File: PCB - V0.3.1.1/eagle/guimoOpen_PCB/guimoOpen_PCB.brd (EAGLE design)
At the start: 45.7 x 73.7 mm, 8 parts, among them M1 ARDUINO-NANO-3.0, U1 GY-521MPU6050

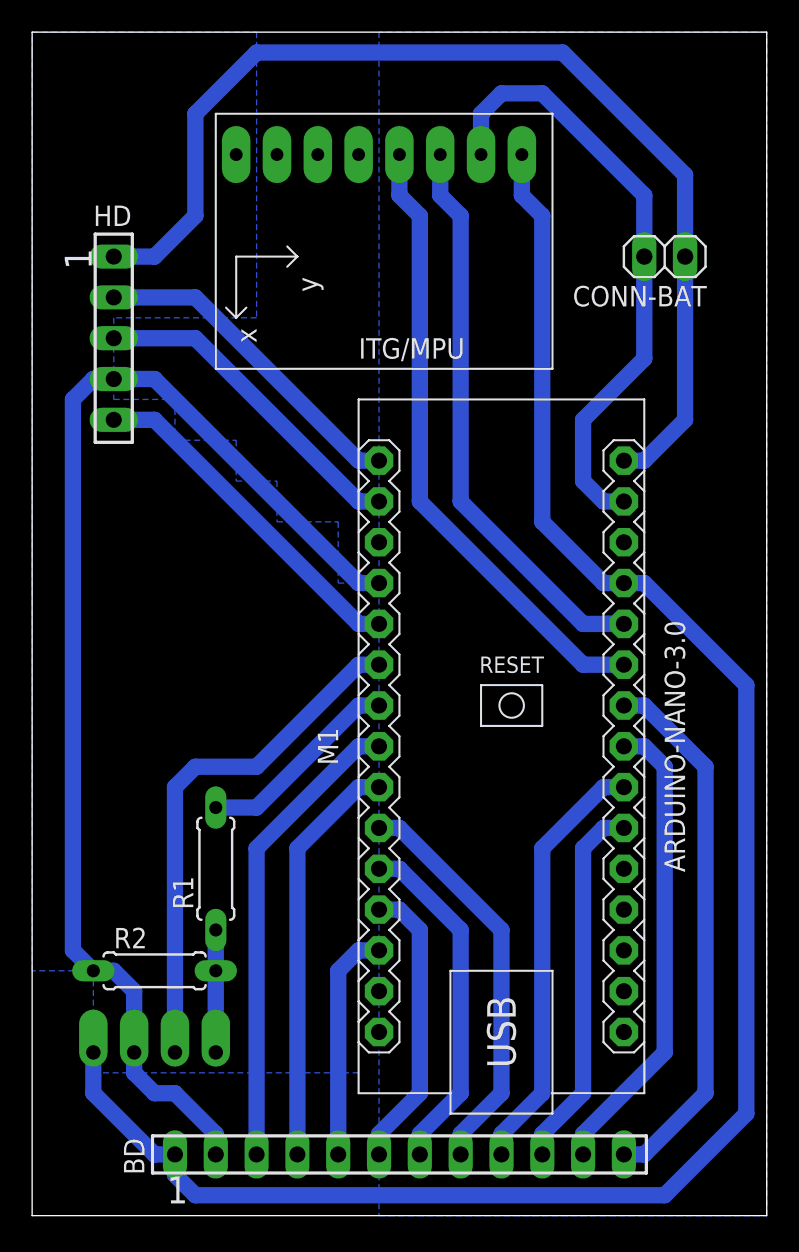
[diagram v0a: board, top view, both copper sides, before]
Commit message: Correção do roteamento do acelerômetro. SDA e SCL foram colocadas nas portas A4 e A5
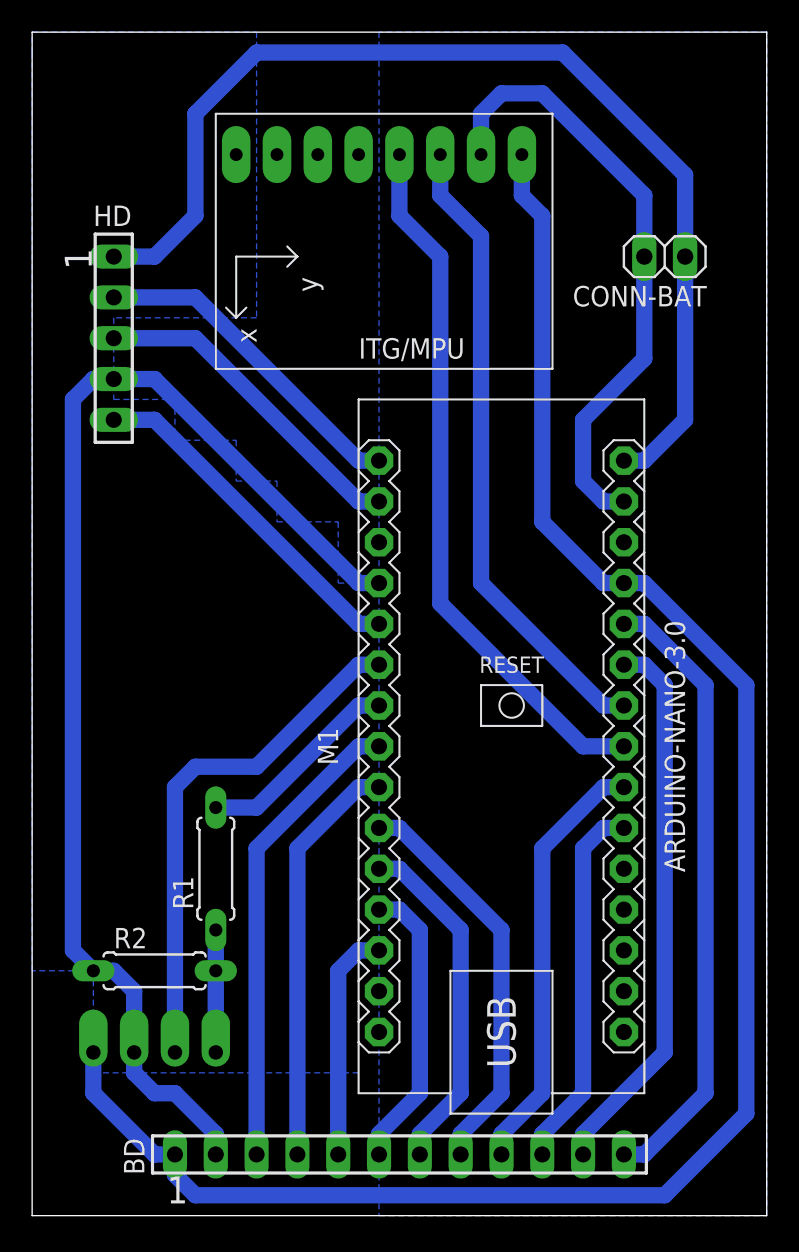
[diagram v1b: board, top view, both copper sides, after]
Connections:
- net N$15: now also M1.J2.5; no longer M1.J2.7
- net N$16: now also M1.J2.6; no longer M1.J2.8
- net N$3: now also M1.J2.7; no longer M1.J2.5
- net N$4: now also M1.J2.8; no longer M1.J2.6
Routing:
- net N$15: track 33.6 -> 38.7 mm
- net N$4: track 39.0 -> 44.1 mm
- net N$16: track 29.3 -> 34.4 mm
- net N$3: track 36.7 -> 39.8 mm
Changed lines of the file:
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@@
 <layer number="17" name="Pads" color="2" fill="1" visible="yes" active="yes"/>
 <layer number="18" name="Vias" color="2" fill="1" visible="yes" active="yes"/>
-<layer number="19" name="Unrouted" color="6" fill="1" visible="yes" active="yes"/>
+<layer number="19" name="Unrouted" color="6" fill="1" visible="no" active="yes"/>
 <layer number="20" name="Dimension" color="15" fill="1" visible="yes" active="yes"/>
-<layer number="21" name="tPlace" color="7" fill="1" visible="yes" active="yes"/>
-<layer number="22" name="bPlace" color="7" fill="1" visible="yes" active="yes"/>
-<layer number="23" name="tOrigins" color="15" fill="1" visible="yes" active="yes"/>
-<layer number="24" name="bOrigins" color="15" fill="1" visible="yes" active="yes"/>
-<layer number="25" name="tNames" color="7" fill="1" visible="yes" active="yes"/>
-<layer number="26" name="bNames" color="7" fill="1" visible="yes" active="yes"/>
-<layer number="27" name="tValues" color="7" fill="1" visible="yes" active="yes"/>
-<layer number="28" name="bValues" color="7" fill="1" visible="yes" active="yes"/>
+<layer number="21" name="tPlace" color="7" fill="1" visible="no" active="yes"/>
+<layer number="22" name="bPlace" color="7" fill="1" visible="no" active="yes"/>
+<layer number="23" name="tOrigins" color="15" fill="1" visible="no" active="yes"/>
+<layer number="24" name="bOrigins" color="15" fill="1" visible="no" active="yes"/>
+<layer number="25" name="tNames" color="7" fill="1" visible="no" active="yes"/>
+<layer number="26" name="bNames" color="7" fill="1" visible="no" active="yes"/>
+<layer number="27" name="tValues" color="7" fill="1" visible="no" active="yes"/>
+<layer number="28" name="bValues" color="7" fill="1" visible="no" active="yes"/>
 <layer number="29" name="tStop" color="7" fill="3" visible="no" active="yes"/>
 <layer number="30" name="bStop" color="7" fill="6" visible="no" active="yes"/>
@@
 <layer number="132" name="bAdjust" color="7" fill="1" visible="no" active="yes"/>
 <layer number="144" name="Drill_legend" color="7" fill="1" visible="no" active="yes"/>
-<layer number="150" name="Notes" color="7" fill="1" visible="yes" active="yes"/>
+<layer number="150" name="Notes" color="7" fill="1" visible="no" active="yes"/>
 <layer number="151" name="HeatSink" color="7" fill="1" visible="no" active="yes"/>
 <layer number="152" name="_bDocu" color="7" fill="1" visible="no" active="yes"/>
@@
 <wire x1="20.32" y1="31.75" x2="21.59" y2="31.75" width="1.016" layer="16"/>
 </signal>
-<signal name="N$4">
-<contactref element="U1" pad="SDA"/>
-<contactref element="M1" pad="J2.6"/>
-<wire x1="36.83" y1="34.29" x2="34.29" y2="34.29" width="1.016" layer="16"/>
-<wire x1="34.29" y1="34.29" x2="24.13" y2="44.45" width="1.016" layer="16"/>
-<wire x1="24.13" y1="44.45" x2="24.13" y2="62.23" width="1.016" layer="16"/>
-<wire x1="24.13" y1="62.23" x2="22.86" y2="63.5" width="1.016" layer="16"/>
-<wire x1="22.86" y1="63.5" x2="22.86" y2="66.04" width="1.016" layer="16"/>
-</signal>
 <signal name="N$7">
 <contactref element="HD" pad="1"/>
@@
 <signal name="N$15">
 <contactref element="BD" pad="12"/>
-<contactref element="M1" pad="J2.7"/>
+<contactref element="M1" pad="J2.5"/>
 <wire x1="36.83" y1="3.81" x2="38.1" y2="3.81" width="1.016" layer="16"/>
 <wire x1="38.1" y1="3.81" x2="41.91" y2="7.62" width="1.016" layer="16"/>
-<wire x1="41.91" y1="7.62" x2="41.91" y2="27.94" width="1.016" layer="16"/>
-<wire x1="41.91" y1="27.94" x2="38.1" y2="31.75" width="1.016" layer="16"/>
-<wire x1="38.1" y1="31.75" x2="36.83" y2="31.75" width="1.016" layer="16"/>
+<wire x1="41.91" y1="7.62" x2="41.91" y2="33.02" width="1.016" layer="16"/>
+<wire x1="41.91" y1="33.02" x2="38.1" y2="36.83" width="1.016" layer="16"/>
+<wire x1="38.1" y1="36.83" x2="36.83" y2="36.83" width="1.016" layer="16"/>
 </signal>
 <signal name="N$16">
 <contactref element="BD" pad="11"/>
-<contactref element="M1" pad="J2.8"/>
+<contactref element="M1" pad="J2.6"/>
 <wire x1="34.29" y1="3.81" x2="34.29" y2="5.08" width="1.016" layer="16"/>
 <wire x1="34.29" y1="5.08" x2="39.37" y2="10.16" width="1.016" layer="16"/>
-<wire x1="39.37" y1="10.16" x2="39.37" y2="27.94" width="1.016" layer="16"/>
-<wire x1="39.37" y1="27.94" x2="38.1" y2="29.21" width="1.016" layer="16"/>
-<wire x1="38.1" y1="29.21" x2="36.83" y2="29.21" width="1.016" layer="16"/>
+<wire x1="39.37" y1="10.16" x2="39.37" y2="33.02" width="1.016" layer="16"/>
+<wire x1="39.37" y1="33.02" x2="38.1" y2="34.29" width="1.016" layer="16"/>
+<wire x1="38.1" y1="34.29" x2="36.83" y2="34.29" width="1.016" layer="16"/>
 </signal>
 <signal name="N$19">
@@
 <wire x1="34.29" y1="22.86" x2="35.56" y2="24.13" width="1.016" layer="16"/>
 <wire x1="35.56" y1="24.13" x2="36.83" y2="24.13" width="1.016" layer="16"/>
-</signal>
-<signal name="N$3">
-<contactref element="U1" pad="SCL"/>
-<contactref element="M1" pad="J2.5"/>
-<wire x1="36.83" y1="36.83" x2="35.56" y2="36.83" width="1.016" layer="16"/>
-<wire x1="25.4" y1="66.04" x2="25.4" y2="63.5" width="1.016" layer="16"/>
-<wire x1="25.4" y1="63.5" x2="26.67" y2="62.23" width="1.016" layer="16"/>
-<wire x1="26.67" y1="62.23" x2="26.67" y2="44.45" width="1.016" layer="16"/>
-<wire x1="26.67" y1="44.45" x2="34.29" y2="36.83" width="1.016" layer="16"/>
-<wire x1="34.29" y1="36.83" x2="36.83" y2="36.83" width="1.016" layer="16"/>
 </signal>
 <signal name="N$17">
@@
 <contactref element="M1" pad="J2.14"/>
 </signal>
+<signal name="N$3">
+<contactref element="U1" pad="SCL"/>
+<contactref element="M1" pad="J2.7"/>
+<wire x1="36.83" y1="31.75" x2="35.56" y2="31.75" width="1.016" layer="16"/>
+<wire x1="35.56" y1="31.75" x2="27.94" y2="39.37" width="1.016" layer="16"/>
+<wire x1="27.94" y1="39.37" x2="27.94" y2="60.96" width="1.016" layer="16"/>
+<wire x1="27.94" y1="60.96" x2="25.4" y2="63.5" width="1.016" layer="16"/>
+<wire x1="25.4" y1="63.5" x2="25.4" y2="66.04" width="1.016" layer="16"/>
+</signal>
+<signal name="N$4">
+<contactref element="U1" pad="SDA"/>
+<contactref element="M1" pad="J2.8"/>
+<wire x1="36.83" y1="29.21" x2="34.29" y2="29.21" width="1.016" layer="16"/>
+<wire x1="34.29" y1="29.21" x2="25.4" y2="38.1" width="1.016" layer="16"/>
+<wire x1="25.4" y1="38.1" x2="25.4" y2="59.69" width="1.016" layer="16"/>
+<wire x1="25.4" y1="59.69" x2="22.86" y2="62.23" width="1.016" layer="16"/>
+<wire x1="22.86" y1="62.23" x2="22.86" y2="66.04" width="1.016" layer="16"/>
+</signal>
 </signals>
